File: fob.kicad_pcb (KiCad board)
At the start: 2 copper layers, 53 x 53 mm, 9 parts, among them P1 SW DBG, P2 SOIC16-ZIF

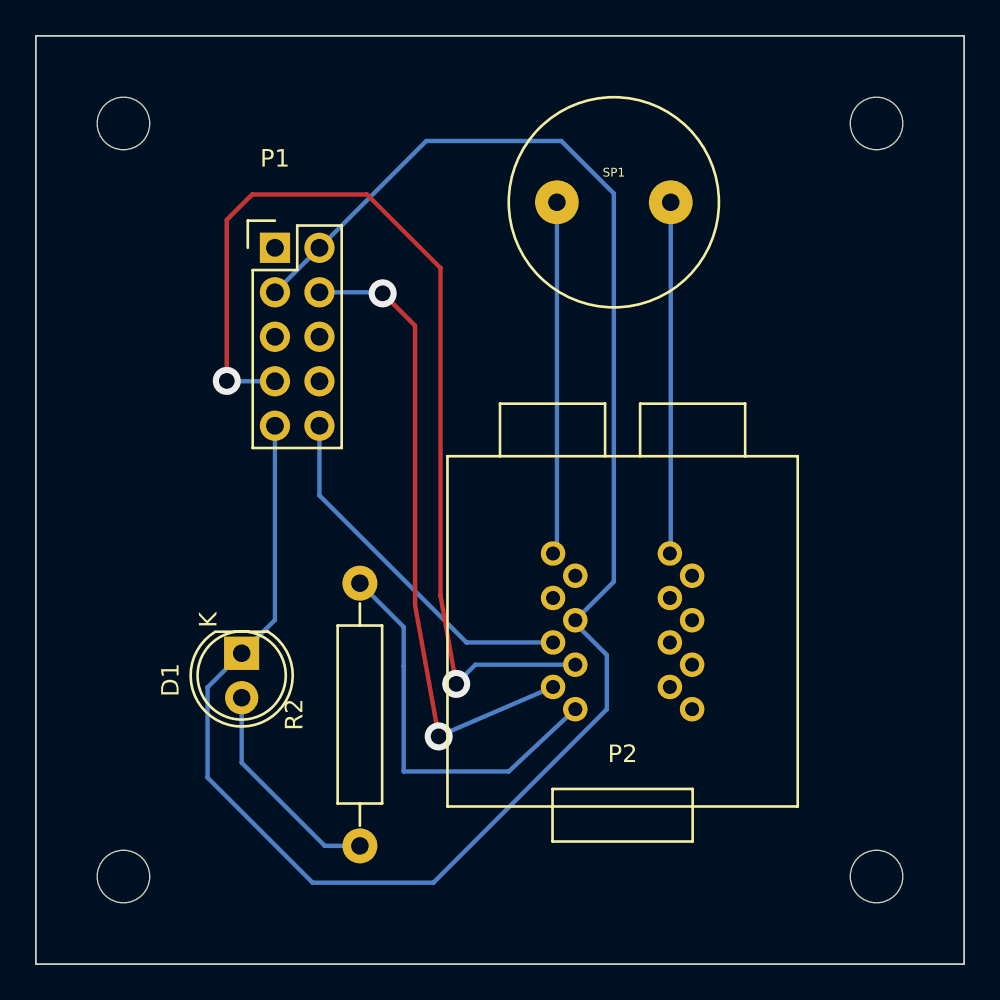
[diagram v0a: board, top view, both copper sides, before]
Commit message: fixed waveshare footprint bug and did relayout
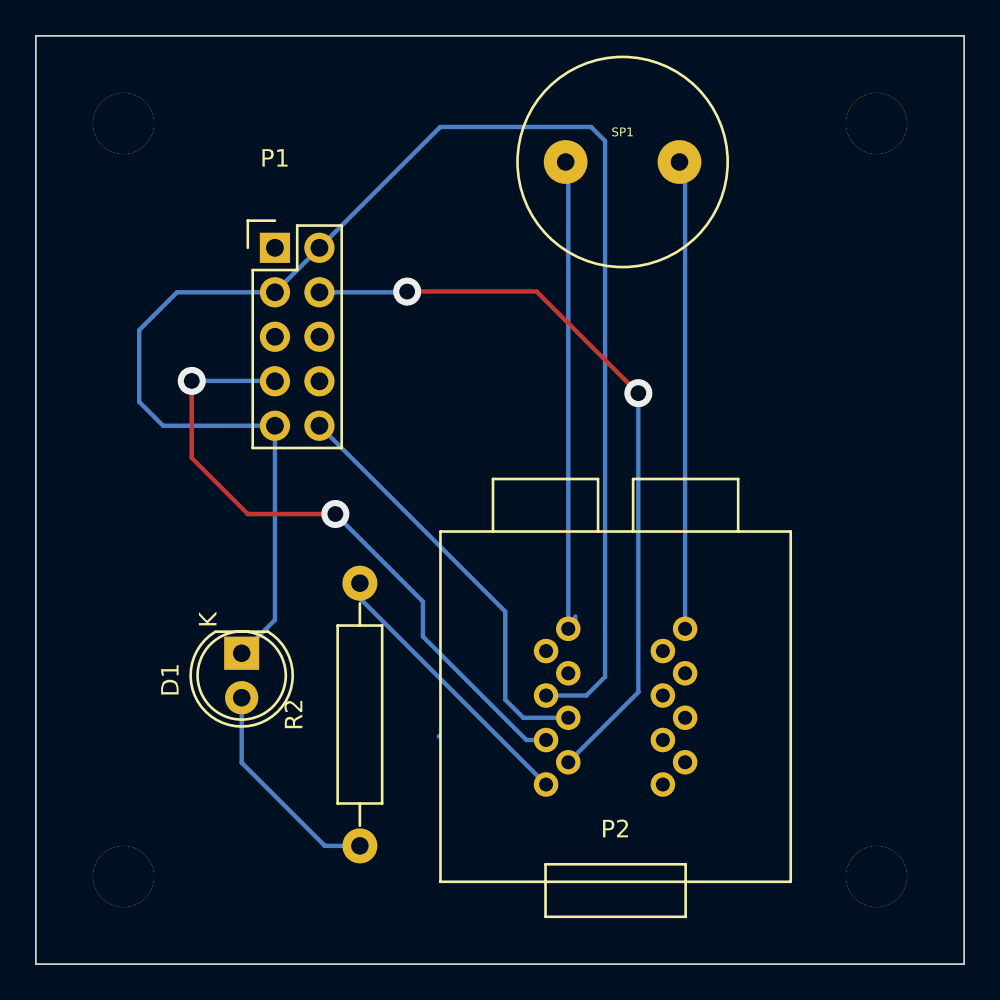
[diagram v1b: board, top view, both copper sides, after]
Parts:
- removed the REF** at (155.0, 80.0)
- removed the REF** at (112.0, 80.0)
- removed the REF** at (112.0, 123.0)
- added REF**: MountingHole_3mm, 3_5_mounting:MountingHole_3_5mm, F.Cu at (112.0, 123.0)
- added REF**: MountingHole_3mm, 3_5_mounting:MountingHole_3_5mm, F.Cu at (112.0, 80.0)
- added REF**: MountingHole_3mm, 3_5_mounting:MountingHole_3_5mm, F.Cu at (155.0, 80.0)
- moved P2 4.32 mm to (140.1, 113.3)
- moved SP1 2.35 mm to (140.5, 82.2)
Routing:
- net Net-(P1-Pad7): track 57.7 -> 37.4 mm
- net GND: track 107.1 -> 92.9 mm
- net Net-(P2-Pad8): track 23.0 -> 15.9 mm
- net Net-(P2-Pad1): track 20.1 -> 27.1 mm
- net Net-(P2-Pad16): track 20.1 -> 26.8 mm
- net Net-(P1-Pad4): track 36.9 -> 43.4 mm
- net VDD: track 20.8 -> 24.1 mm

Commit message: got version 1.1 ready to cut
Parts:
- added R1: 10K, Resistors_ThroughHole:Resistor_Horizontal_RM15mm, F.Cu at (128.5, 96.5)
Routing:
- net VDD: track 24.1 -> 48.7 mm
- net Net-(P1-Pad7): track 37.4 -> 52.9 mm
- net Net-(P1-Pad4): track 43.4 -> 47.9 mm
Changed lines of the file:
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@@
 (kicad_pcb (version 4) (host pcbnew "(2015-06-01 BZR 5694)-product")
   (general
-    (links 11)
+    (links 13)
     (no_connects 0)
-    (area 106.949999 74.949999 160.050001 128.050001)
+    (area 105.511474 74.8745 163.490046 128.97626)
     (thickness 1.6)
     (drawings 4)
-    (tracks 51)
+    (tracks 62)
     (zones 0)
-    (modules 9)
+    (modules 10)
     (nets 13)
   )
@@
     (title "Form Of Bee")
     (date "Wed 26 Aug 2015")
-    (rev 1.0b)
+    (rev 1.1)
     (company "Bart Massey")
     (comment 1 "Copyright 2015 Bart Massey")
@@
     (pad "" thru_hole circle (at 0 0) (size 3.5 3.5) (drill 3.5) (layers *.Cu *.Mask F.SilkS))
   )
+  (module Resistors_ThroughHole:Resistor_Horizontal_RM15mm (layer F.Cu)
+    (at 128.5 96.5 90)
+    (descr "Resistor, Axial, RM 15mm,")
+    (tags "Resistor, Axial, RM 15mm,")
+    (fp_text reference R1 (at 0 -3.74904 90) (layer F.SilkS)
+      (effects (font (size 1 1) (thickness 0.15)))
+    )
+    (fp_text value 10K (at 0 4.0005 90) (layer F.Fab)
+      (effects (font (size 1 1) (thickness 0.15)))
+    )
+    (fp_line (start -5.08 -1.27) (end -5.08 1.27) (layer F.SilkS) (width 0.15))
+    (fp_line (start -5.08 1.27) (end 5.08 1.27) (layer F.SilkS) (width 0.15))
+    (fp_line (start 5.08 1.27) (end 5.08 -1.27) (layer F.SilkS) (width 0.15))
+    (fp_line (start 5.08 -1.27) (end -5.08 -1.27) (layer F.SilkS) (width 0.15))
+    (fp_line (start 6.35 0) (end 5.08 0) (layer F.SilkS) (width 0.15))
+    (fp_line (start -6.35 0) (end -5.08 0) (layer F.SilkS) (width 0.15))
+    (pad 1 thru_hole circle (at -7.5 0 90) (size 1.99898 1.99898) (drill 1.00076) (layers *.Cu *.SilkS *.Mask)
+      (net 9 VDD))
+    (pad 2 thru_hole circle (at 7.5 0 90) (size 1.99898 1.99898) (drill 1.00076) (layers *.Cu *.SilkS *.Mask)
+      (net 7 "Net-(P1-Pad7)"))
+    (model Resistors_ThroughHole.3dshapes/Resistor_Horizontal_RM15mm.wrl
+      (at (xyz 0 0 0))
+      (scale (xyz 0.4 0.4 0.4))
+      (rotate (xyz 0 0 0))
+    )
+  )
   (gr_line (start 107 128) (end 107 75) (angle 90) (layer Edge.Cuts) (width 0.1))
   (gr_line (start 160 128) (end 107 128) (angle 90) (layer Edge.Cuts) (width 0.1))
@@
   (segment (start 118.75 116.5) (end 118.75 112.79) (width 0.25) (layer B.Cu) (net 2))
   (segment (start 123.5 121.25) (end 118.75 116.5) (width 0.25) (layer B.Cu) (net 2))
+  (segment (start 141.4 95.4) (end 141.4 94.9) (width 0.25) (layer F.Cu) (net 4))
+  (segment (start 137.4 116.475) (end 141.4 112.475) (width 0.25) (layer B.Cu) (net 4))
+  (via (at 141.4 95.4) (size 1.6) (drill 0.9) (layers F.Cu B.Cu) (net 4))
   (segment (start 141.4 112.475) (end 141.4 95.4) (width 0.25) (layer B.Cu) (net 4))
-  (via (at 141.4 95.4) (size 1.6) (drill 0.9) (layers F.Cu B.Cu) (net 4))
-  (segment (start 141.4 95.4) (end 135.6 89.6) (width 0.25) (layer F.Cu) (net 4))
-  (segment (start 135.6 89.6) (end 128.2 89.6) (width 0.25) (layer F.Cu) (net 4))
-  (via (at 128.2 89.6) (size 1.6) (drill 0.9) (layers F.Cu B.Cu) (net 4))
-  (segment (start 128.2 89.6) (end 128.16 89.64) (width 0.25) (layer B.Cu) (net 4))
-  (segment (start 128.16 89.64) (end 123.19 89.64) (width 0.25) (layer B.Cu) (net 4))
-  (segment (start 137.4 116.475) (end 141.4 112.475) (width 0.25) (layer B.Cu) (net 4))
+  (segment (start 128.33 84.5) (end 123.19 89.64) (width 0.25) (layer B.Cu) (net 4))
+  (segment (start 131 84.5) (end 128.33 84.5) (width 0.25) (layer B.Cu) (net 4))
+  (via (at 131 84.5) (size 0.6) (layers F.Cu B.Cu) (net 4))
+  (segment (start 141.4 94.9) (end 131 84.5) (width 0.25) (layer F.Cu) (net 4))
+  (segment (start 128.5 89) (end 128.5 98.5) (width 0.25) (layer B.Cu) (net 7))
+  (segment (start 124.7 102.3) (end 124.1 102.3) (width 0.25) (layer B.Cu) (net 7))
+  (segment (start 128.5 98.5) (end 124.7 102.3) (width 0.25) (layer B.Cu) (net 7))
   (segment (start 120.65 94.72) (end 120.53 94.72) (width 0.25) (layer B.Cu) (net 7))
   (segment (start 120.63 94.7) (end 120.65 94.72) (width 0.25) (layer B.Cu) (net 7))
@@
   (segment (start 135.005 115.205) (end 129.1 109.3) (width 0.25) (layer B.Cu) (net 7))
   (segment (start 120.63 94.7) (end 115.9 94.7) (width 0.25) (layer B.Cu) (net 7))
-  (segment (start 134.835 113.935) (end 133.8 112.9) (width 0.25) (layer B.Cu) (net 9))
-  (segment (start 133.8 112.9) (end 133.8 107.87) (width 0.25) (layer B.Cu) (net 9))
-  (segment (start 133.8 107.87) (end 123.19 97.26) (width 0.25) (layer B.Cu) (net 9))
-  (segment (start 137.4 113.935) (end 134.835 113.935) (width 0.25) (layer B.Cu) (net 9))
+  (segment (start 128.2 89.6) (end 128.16 89.64) (width 0.25) (layer B.Cu) (net 7))
+  (segment (start 128.5 104) (end 131.5 101) (width 0.25) (layer B.Cu) (net 9))
+  (segment (start 125.5 94.95) (end 123.19 97.26) (width 0.25) (layer B.Cu) (net 9))
+  (segment (start 125.5 88.5) (end 125.5 94.95) (width 0.25) (layer B.Cu) (net 9))
+  (segment (start 127 87) (end 125.5 88.5) (width 0.25) (layer B.Cu) (net 9))
+  (segment (start 130 87) (end 127 87) (width 0.25) (layer B.Cu) (net 9))
+  (segment (start 131.5 88.5) (end 130 87) (width 0.25) (layer B.Cu) (net 9))
+  (segment (start 131.5 101) (end 131.5 88.5) (width 0.25) (layer B.Cu) (net 9))
+  (segment (start 137.4 113.935) (end 135.065 113.935) (width 0.25) (layer B.Cu) (net 9))
+  (segment (start 131 106.5) (end 128.5 104) (width 0.25) (layer B.Cu) (net 9))
+  (segment (start 131 109.87) (end 131 106.5) (width 0.25) (layer B.Cu) (net 9))
+  (segment (start 135.065 113.935) (end 131 109.87) (width 0.25) (layer B.Cu) (net 9))
   (segment (start 137.8 108.365) (end 137.8 108.15) (width 0.25) (layer B.Cu) (net 10))
   (segment (start 137.8 108.365) (end 137.8 108.55) (width 0.25) (layer B.Cu) (net 10))
